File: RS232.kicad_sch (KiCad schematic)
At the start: 5 parts, among them U4 MAX3232

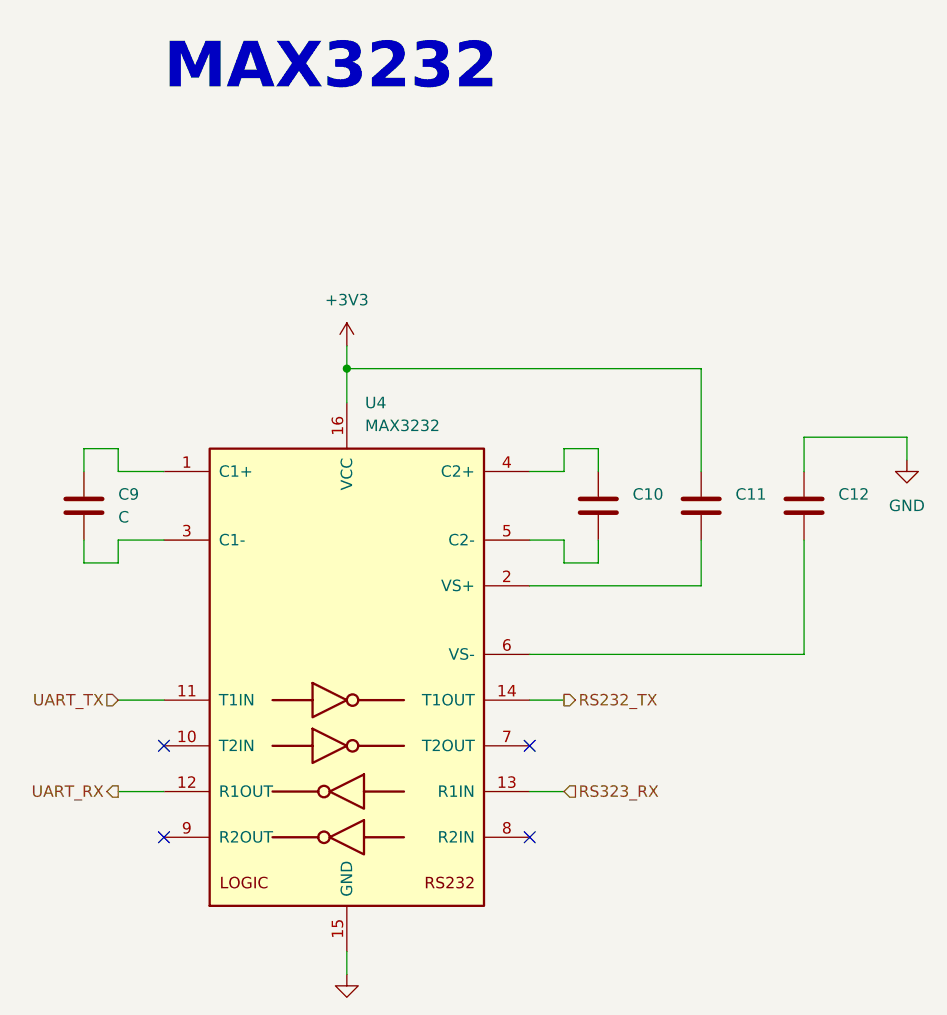
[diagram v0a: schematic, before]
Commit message: parcialmente terminada PCB falta verificar tamano de componentes
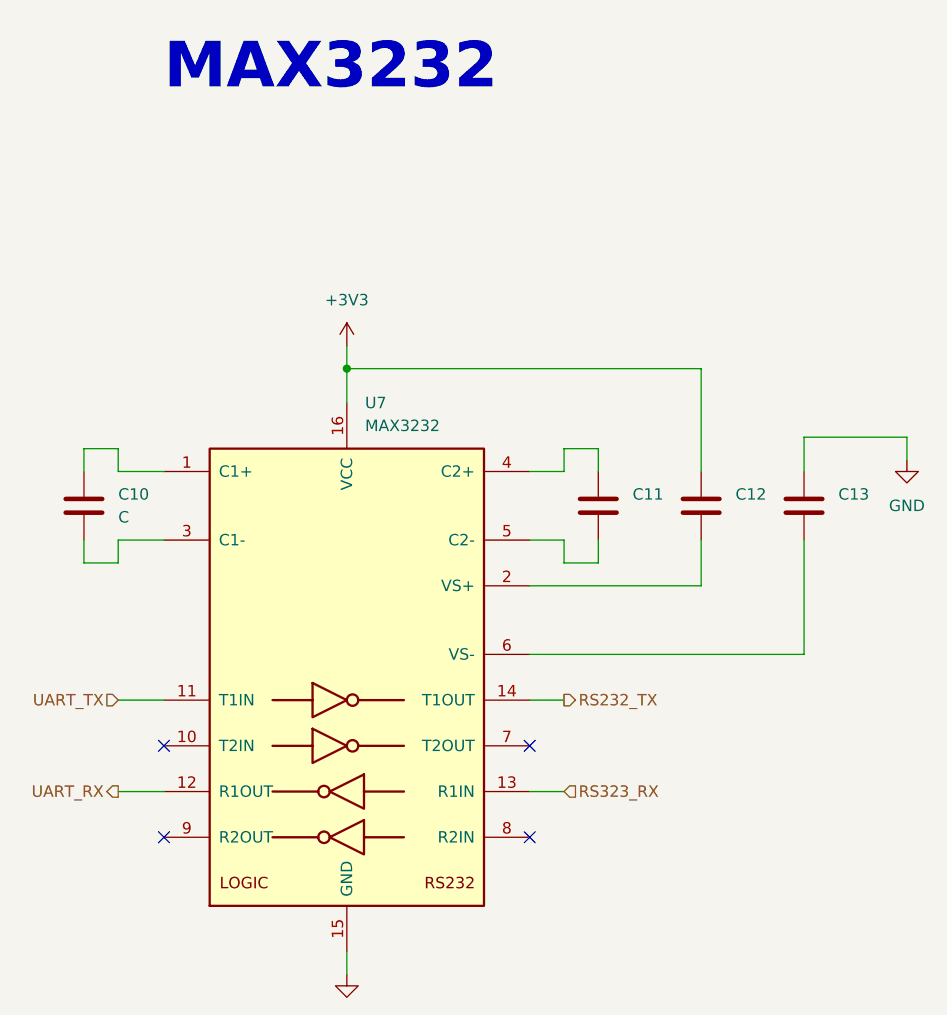
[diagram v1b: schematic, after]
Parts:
- C10: renamed from C9; footprint (none) -> Capacitor_SMD:C_0603_1608Metric
- C11: renamed from C10; value (none) -> ~; footprint (none) -> Capacitor_SMD:C_0603_1608Metric
- C12: renamed from C11; value (none) -> ~; footprint (none) -> Capacitor_SMD:C_0603_1608Metric
- C13: renamed from C12; value (none) -> ~; footprint (none) -> Capacitor_SMD:C_0603_1608Metric
- U7: renamed from U4; footprint (none) -> Package_SO:SSOP-20_3.9x8.7mm_P0.635mm
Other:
- title: (none) -> GPS_CHECK
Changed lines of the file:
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@@
 (kicad_sch (version 20211123) (generator eeschema)
   (paper "A4")
+  (title_block
+    (title "GPS_CHECK")
+    (date "2022-04-10")
+    (rev "v1.0.0")
+  )
   (junction (at 149.86 60.96) (diameter 0) (color 0 0 0 0)
   )
@@
   (symbol (lib_id "Device:C") (at 177.8 76.2 0) (unit 1)
     (in_bom yes) (on_board yes) (fields_autoplaced)
-    (property "Reference" "C10" (id 0) (at 181.61 74.9299 0)
-      (effects (font (size 1.27 1.27)) (justify left))
-    )
-    (property "Value" "" (id 1) (at 181.61 77.4699 0)
-      (effects (font (size 1.27 1.27)) (justify left))
-    )
-    (property "Footprint" "" (id 2) (at 178.7652 80.01 0)
+    (property "Reference" "C11" (id 0) (at 181.61 74.9299 0)
+      (effects (font (size 1.27 1.27)) (justify left))
+    )
+    (property "Value" "~" (id 1) (at 181.61 77.4699 0)
+      (effects (font (size 1.27 1.27)) (justify left))
+    )
+    (property "Footprint" "Capacitor_SMD:C_0603_1608Metric" (id 2) (at 178.7652 80.01 0)
       (effects (font (size 1.27 1.27)) hide)
     )
@@
   (symbol (lib_id "Device:C") (at 189.23 76.2 0) (unit 1)
     (in_bom yes) (on_board yes) (fields_autoplaced)
-    (property "Reference" "C11" (id 0) (at 193.04 74.9299 0)
-      (effects (font (size 1.27 1.27)) (justify left))
-    )
-    (property "Value" "" (id 1) (at 193.04 77.4699 0)
-      (effects (font (size 1.27 1.27)) (justify left))
-    )
-    (property "Footprint" "" (id 2) (at 190.1952 80.01 0)
+    (property "Reference" "C12" (id 0) (at 193.04 74.9299 0)
+      (effects (font (size 1.27 1.27)) (justify left))
+    )
+    (property "Value" "~" (id 1) (at 193.04 77.4699 0)
+      (effects (font (size 1.27 1.27)) (justify left))
+    )
+    (property "Footprint" "Capacitor_SMD:C_0603_1608Metric" (id 2) (at 190.1952 80.01 0)
       (effects (font (size 1.27 1.27)) hide)
     )
@@
   (symbol (lib_id "Device:C") (at 200.66 76.2 0) (unit 1)
     (in_bom yes) (on_board yes) (fields_autoplaced)
-    (property "Reference" "C12" (id 0) (at 204.47 74.9299 0)
-      (effects (font (size 1.27 1.27)) (justify left))
-    )
-    (property "Value" "" (id 1) (at 204.47 77.4699 0)
-      (effects (font (size 1.27 1.27)) (justify left))
-    )
-    (property "Footprint" "" (id 2) (at 201.6252 80.01 0)
+    (property "Reference" "C13" (id 0) (at 204.47 74.9299 0)
+      (effects (font (size 1.27 1.27)) (justify left))
+    )
+    (property "Value" "~" (id 1) (at 204.47 77.4699 0)
+      (effects (font (size 1.27 1.27)) (justify left))
+    )
+    (property "Footprint" "Capacitor_SMD:C_0603_1608Metric" (id 2) (at 201.6252 80.01 0)
       (effects (font (size 1.27 1.27)) hide)
     )
@@
   (symbol (lib_id "power:GND") (at 212.09 71.12 0) (unit 1)
     (in_bom yes) (on_board yes) (fields_autoplaced)
-    (property "Reference" "#PWR0126" (id 0) (at 212.09 77.47 0)
+    (property "Reference" "#PWR030" (id 0) (at 212.09 77.47 0)
       (effects (font (size 1.27 1.27)) hide)
     )
@@
   (symbol (lib_id "power:GND") (at 149.86 128.27 0) (unit 1)
     (in_bom yes) (on_board yes) (fields_autoplaced)
-    (property "Reference" "#PWR0125" (id 0) (at 149.86 134.62 0)
+    (property "Reference" "#PWR029" (id 0) (at 149.86 134.62 0)
       (effects (font (size 1.27 1.27)) hide)
     )
@@
   (symbol (lib_id "Interface_UART:MAX3232") (at 149.86 95.25 0) (unit 1)
     (in_bom yes) (on_board yes) (fields_autoplaced)
-    (property "Reference" "U4" (id 0) (at 151.8794 64.77 0)
+    (property "Reference" "U7" (id 0) (at 151.8794 64.77 0)
       (effects (font (size 1.27 1.27)) (justify left))
     )
@@
       (effects (font (size 1.27 1.27)) (justify left))
     )
-    (property "Footprint" "" (id 2) (at 151.13 121.92 0)
+    (property "Footprint" "Package_SO:SSOP-20_3.9x8.7mm_P0.635mm" (id 2) (at 151.13 121.92 0)
       (effects (font (size 1.27 1.27)) (justify left) hide)
     )
@@
   (symbol (lib_id "power:+3V3") (at 149.86 58.42 0) (unit 1)
     (in_bom yes) (on_board yes) (fields_autoplaced)
-    (property "Reference" "#PWR0127" (id 0) (at 149.86 62.23 0)
+    (property "Reference" "#PWR028" (id 0) (at 149.86 62.23 0)
       (effects (font (size 1.27 1.27)) hide)
     )
@@
   (symbol (lib_id "Device:C") (at 120.65 76.2 0) (unit 1)
     (in_bom yes) (on_board yes) (fields_autoplaced)
-    (property "Reference" "C9" (id 0) (at 124.46 74.9299 0)
+    (property "Reference" "C10" (id 0) (at 124.46 74.9299 0)
       (effects (font (size 1.27 1.27)) (justify left))
     )
@@
       (effects (font (size 1.27 1.27)) (justify left))
     )
-    (property "Footprint" "" (id 2) (at 121.6152 80.01 0)
-      (effects (font (size 1.27 1.27)) hide)
-    )
+    (property "Footprint" "Capacitor_SMD:C_0603_1608Metric" (id 2) (at 121.6152 80.01 0)
+      (effects (font (size 1.27 1.27)) hide)
+    )

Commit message: terminando, aun falta una ultima revision previa a la fabricacion
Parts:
- U7: footprint Package_SO:SSOP-20_3.9x8.7mm_P0.635mm -> Package_SO:SOIC-16_4.55x10.3mm_P1.27mm
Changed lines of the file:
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@@
       (effects (font (size 1.27 1.27)) (justify left))
     )
-    (property "Footprint" "Package_SO:SSOP-20_3.9x8.7mm_P0.635mm" (id 2) (at 151.13 121.92 0)
+    (property "Footprint" "Package_SO:SOIC-16_4.55x10.3mm_P1.27mm" (id 2) (at 151.13 121.92 0)
       (effects (font (size 1.27 1.27)) (justify left) hide)
     )
